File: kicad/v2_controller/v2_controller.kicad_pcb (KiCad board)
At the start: 2 copper layers, 100 x 116 mm, 131 parts, among them J1 Conn_02x10_Odd_Even, J2 Conn_02x10_Odd_Even, J3 USB_C_Receptacle_USB2.0, J4 USB_C_Receptacle_USB2.0, J5 Conn_02x04_Odd_Even, Q1 S8050, Q2 S8050, SW18 Boot, SW19 Reset, U1 ESP32-S3-WROOM-1-N16R8, U2 SSD1306_I2C, U3 74AHCT1G125, U4 AMS1117-3.3, U5 USBLC6-2P6, U6 USBLC6-2P6, U7 CP2102N-Axx-xQFN24

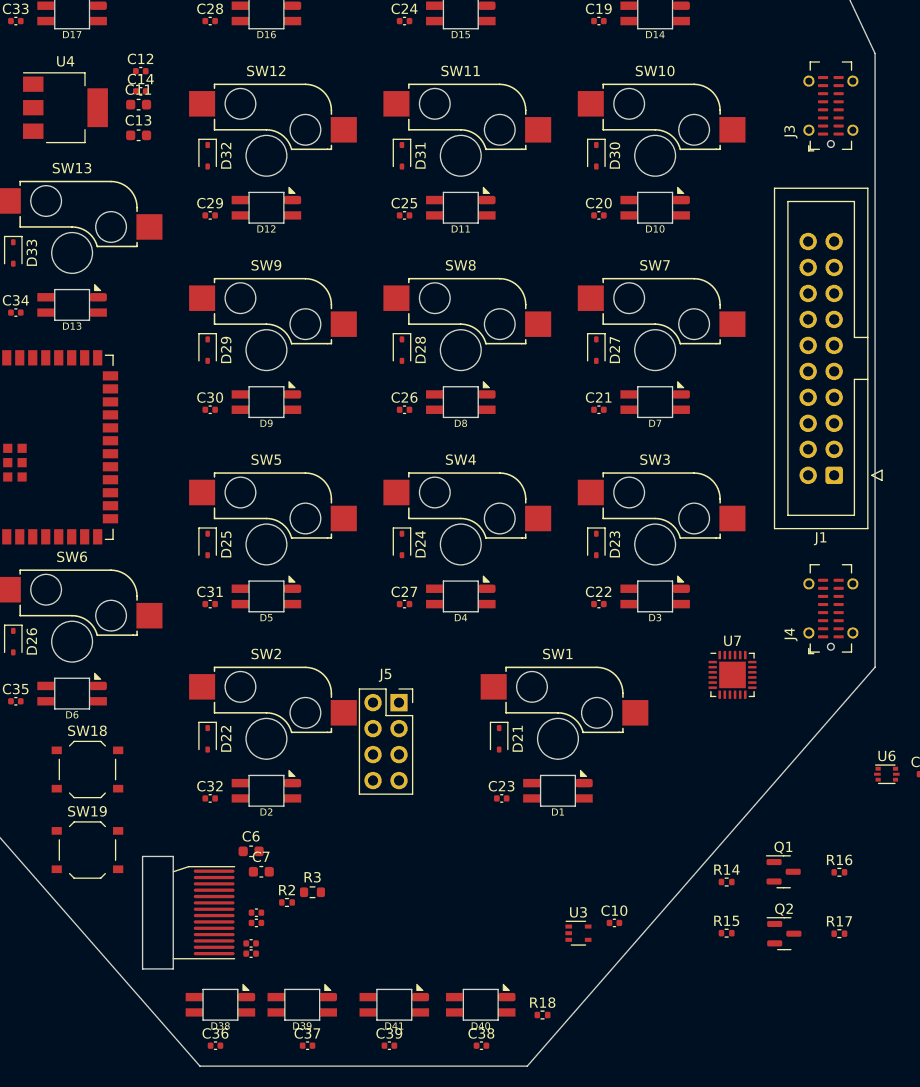
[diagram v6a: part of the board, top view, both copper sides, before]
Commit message: [kicad] more v2 controller PCB tweaks
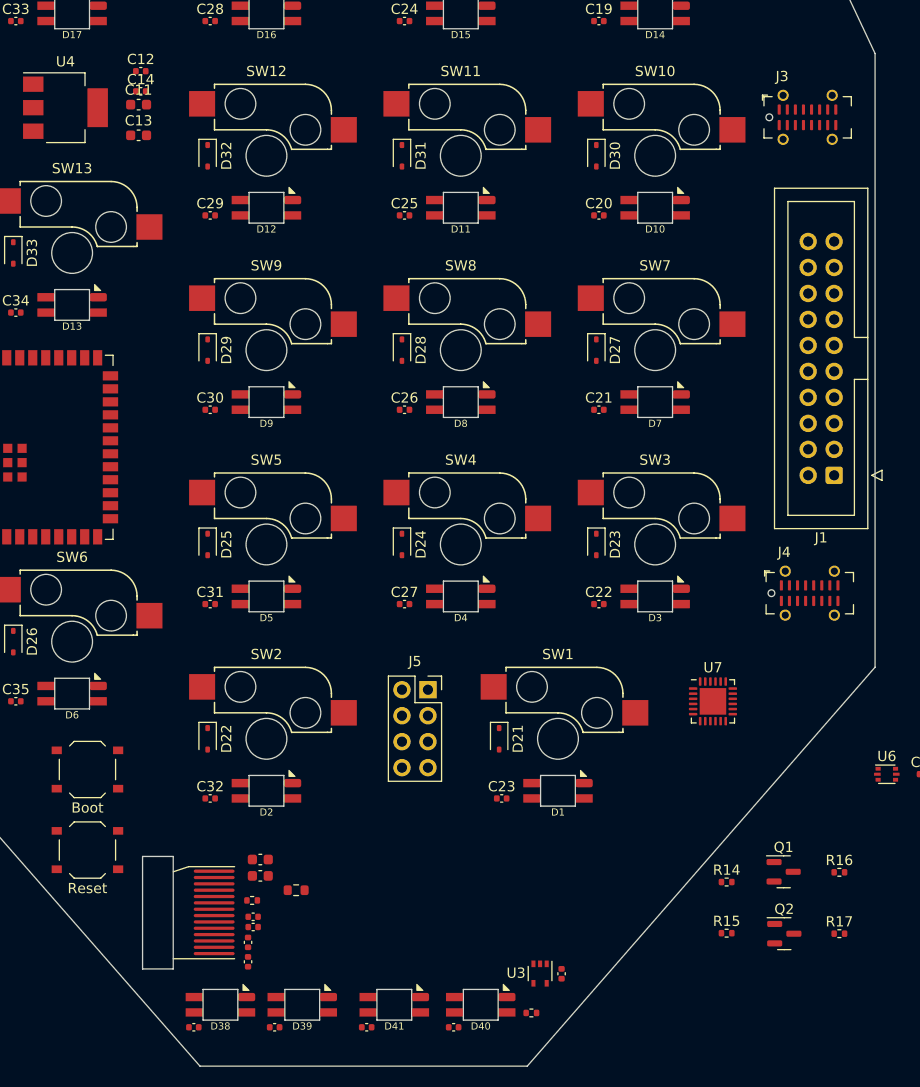
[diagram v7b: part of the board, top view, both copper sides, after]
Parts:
- moved C10 7.17 mm to (109.3, 147.0), turned to 90 degrees
- moved U3 5.45 mm to (107.2, 146.9), turned to -90 degrees
- moved C37 3.69 mm to (81.3, 152.2)
- moved R2 3.42 mm to (79.1, 139.8), turned to 180 degrees
- moved C38 3.26 mm to (98.8, 152.2)
- moved U7 3.22 mm to (124.2, 120.3)
- moved J5 3.10 mm to (96.3, 119.2)
- moved C39 2.86 mm to (90.3, 152.2)
- moved C36 2.78 mm to (73.4, 152.2)
- moved J4 2.54 mm to (133.6, 109.8), turned to 0 degrees
- moved J3 2.54 mm to (133.4, 63.2), turned to 0 degrees
- moved R3 1.61 mm to (83.4, 138.8)
- moved C6 1.20 mm to (79.9, 135.8)
- moved R18 1.11 mm to (106.4, 150.8)
- moved C9 0.85 mm to (78.7, 145.8), turned to -90 degrees
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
